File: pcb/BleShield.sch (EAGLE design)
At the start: 11 parts, among them U1 ARDUINO_SHIELDNOHOLES, Y1 32.768KHz, 10PPM

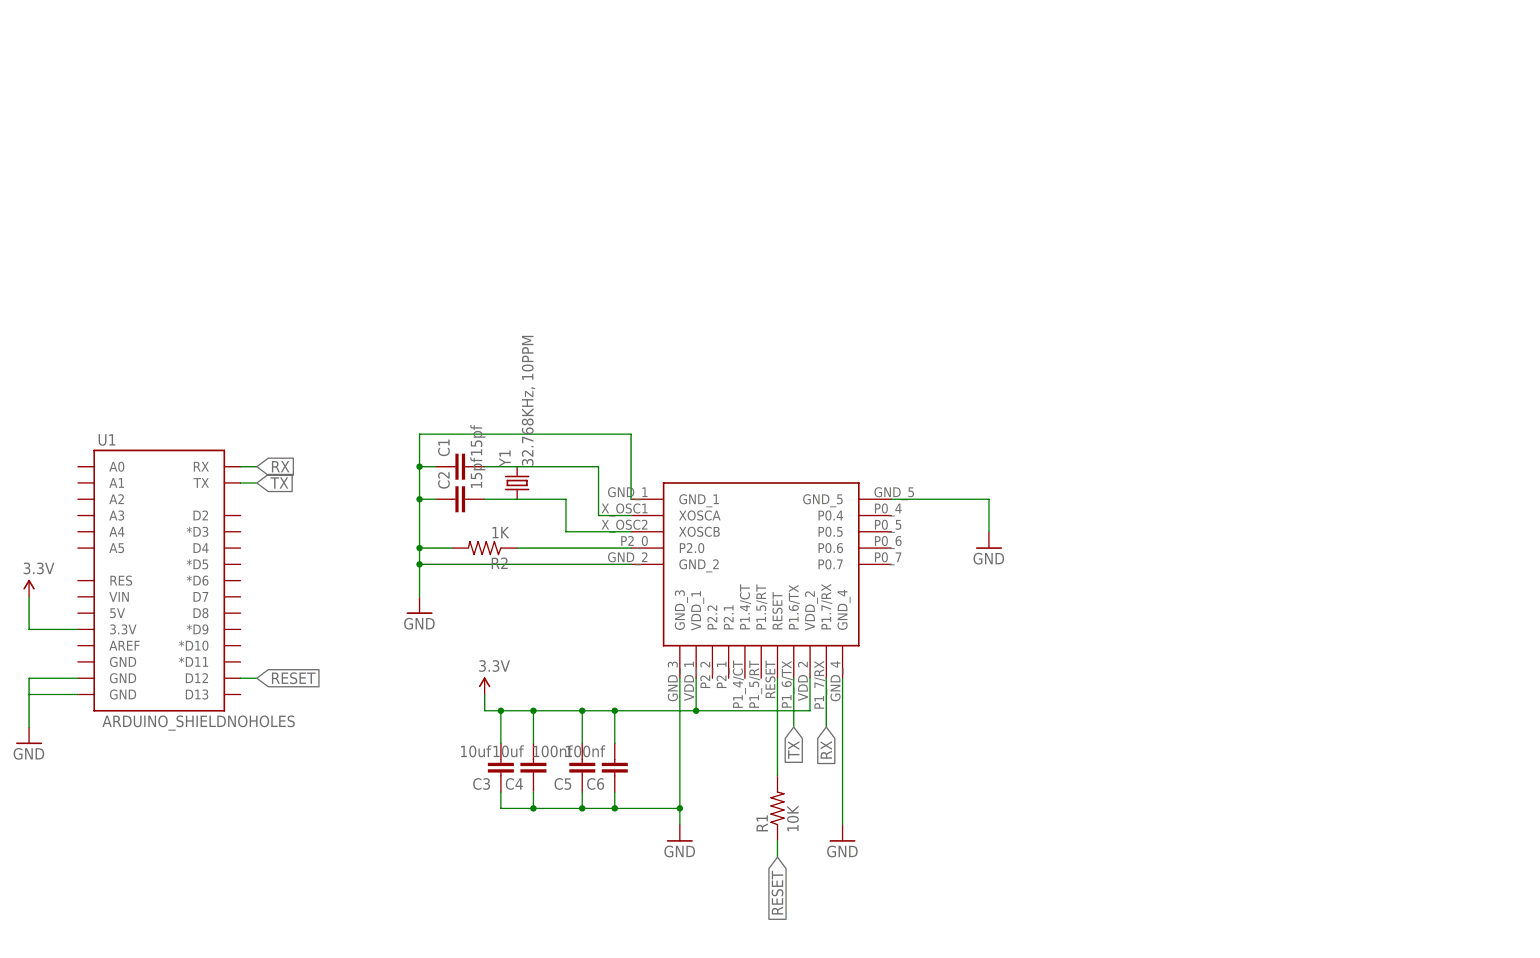
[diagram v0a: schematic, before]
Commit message: Add option to use software serial port, make the board smaller, etc.
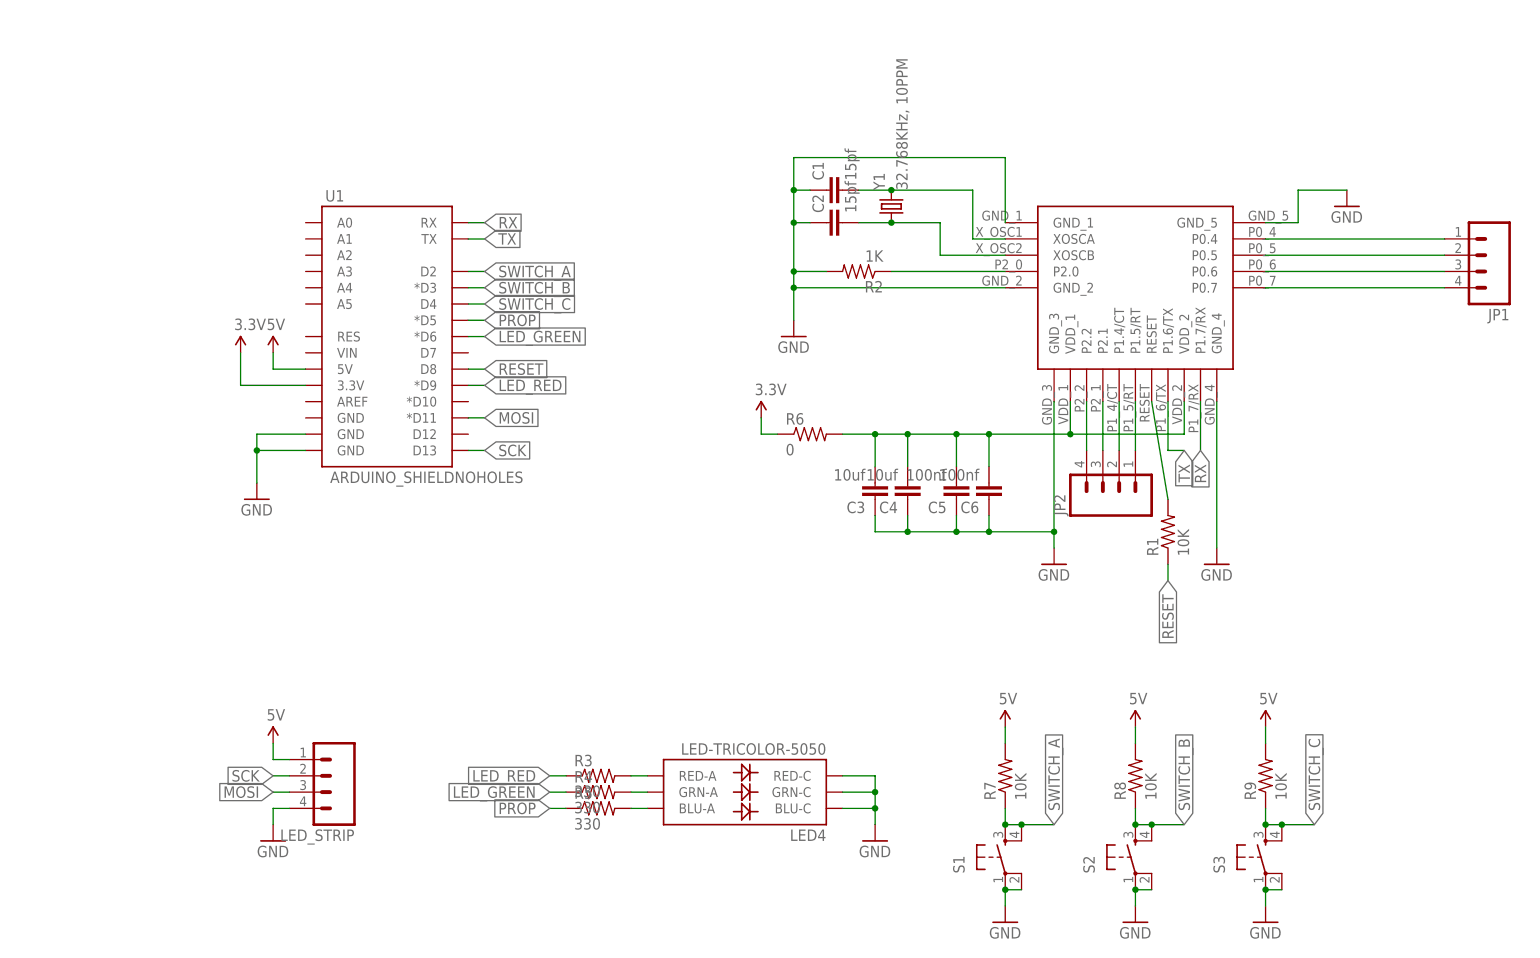
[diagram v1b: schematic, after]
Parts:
- added JP1, JP2, LED_STRIP: (no value), SparkFun:M04PTH
- added LED4: LED-TRICOLOR-5050, SparkFun:LED-TRICOLOR-5050
- added R3, R4, R5: 330, SparkFun:RESISTOR0805-RES
- added R6: 0, SparkFun:RESISTOR0805-RES
- added R7, R8, R9: 10K, SparkFun:RESISTOR0805-RES
- added S1, S2, S3: (no value), SparkFun:TAC_SWITCHSMD
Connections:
- new net 5V: LED_STRIP.1, R7.2, R8.2, R9.2, U1.5V
- new net LED_GREEN: R4.1, U1.*D6
- new net LED_RED: R3.1, U1.*D9
- new net MOSI: LED_STRIP.3, U1.*D11
- new net N$10: JP1.2, U$1.P0.5
- new net N$11: JP1.3, U$1.P0.6
- new net N$12: JP1.4, U$1.P0.7
- new net N$13: JP2.1, U$1.P1.5/RT
- new net N$14: JP2.2, U$1.P1.4/CT
- new net N$15: JP2.3, U$1.P2.1
- new net N$16: JP2.4, U$1.P2.2
- new net N$5: LED4.RED-A, R3.2
- new net N$6: LED4.GRN-A, R4.2
- new net N$7: LED4.BLU-A, R5.2
- new net N$8: C3.2, C4.2, C5.2, C6.2, R6.2, U$1.VDD_1, U$1.VDD_2
- new net N$9: JP1.1, U$1.P0.4
- new net PROP: R5.1, U1.*D5
- new net SCK: LED_STRIP.2, U1.D13
- new net SWITCH_A: R7.1, S1.3, S1.4, U1.D2
- new net SWITCH_B: R8.1, S2.3, S2.4, U1.*D3
- new net SWITCH_C: R9.1, S3.3, S3.4, U1.D4
- net 3.3V: now also R6.1; no longer C3.2, C4.2, C5.2, C6.2, U$1.VDD_1, U$1.VDD_2
- net GND: now also LED4.BLU-C, LED4.GRN-C, LED4.RED-C, LED_STRIP.4, S1.1, S1.2, S2.1, S2.2, S3.1, S3.2
- net RESET: now also U1.D8; no longer U1.D12
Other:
- moved on the sheet: C1, C2, C3, C4, C5, C6, R1, R2, U1, Y1

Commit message: label most of the things
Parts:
- added R10, R11: 0 DNP, SparkFun:RESISTOR0805-RES
- added R12, R13: 0, SparkFun:RESISTOR0805-RES
- JP0: value (none) -> LED_STRIP
- S1: value (none) -> A
- renumbered LED_STRIP to JP0, S2 to B, S3 to C
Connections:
- net PROP renamed LED_BLUE
- new net N$18: R10.2, U1.D2
- new net N$19: R12.2, U1.RX
- new net N$20: R13.2, U1.TX
- new net N$21: R11.2, U1.*D3
- net RX: now also R10.1, R12.1; no longer U1.RX
- net SWITCH_A: now also U1.D4; no longer U1.D2
- net SWITCH_B: now also U1.D12; no longer U1.*D3
- net SWITCH_C: now also U1.D7; no longer U1.D4
- net TX: now also R11.1, R13.1; no longer U1.TX

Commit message: Remove R2 resistor
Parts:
- removed R2: 1K, SparkFun:RESISTOR0805-RES
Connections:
- removed net N$2: R2.1, U$1.P2.0
- net GND: no longer R2.2
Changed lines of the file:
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@@
 <?xml version="1.0" encoding="utf-8"?>
 <!DOCTYPE eagle SYSTEM "eagle.dtd">
-<eagle version="6.2">
+<eagle version="6.4">
 <drawing>
 <settings>
@@
 <part name="GND3" library="SparkFun" deviceset="GND" device=""/>
 <part name="R1" library="SparkFun" deviceset="RESISTOR" device="0805-RES" value="10K"/>
-<part name="R2" library="SparkFun" deviceset="RESISTOR" device="0805-RES" value="1K"/>
 <part name="GND4" library="SparkFun" deviceset="GND" device=""/>
 <part name="GND5" library="SparkFun" deviceset="GND" device=""/>
@@
 <instance part="GND3" gate="1" x="101.6" y="99.06"/>
 <instance part="R1" gate="G$1" x="160.02" y="68.58" rot="R90"/>
-<instance part="R2" gate="G$1" x="111.76" y="109.22" rot="R180"/>
 <instance part="GND4" gate="1" x="187.96" y="119.38"/>
 <instance part="GND5" gate="1" x="167.64" y="63.5"/>
@@
 <wire x1="101.6" y1="127" x2="101.6" y2="121.92" width="0.1524" layer="91"/>
 <junction x="101.6" y="106.68"/>
-<pinref part="R2" gate="G$1" pin="2"/>
 <wire x1="101.6" y1="121.92" x2="101.6" y2="116.84" width="0.1524" layer="91"/>
-<wire x1="101.6" y1="116.84" x2="101.6" y2="109.22" width="0.1524" layer="91"/>
-<wire x1="101.6" y1="109.22" x2="101.6" y2="106.68" width="0.1524" layer="91"/>
-<wire x1="106.68" y1="109.22" x2="101.6" y2="109.22" width="0.1524" layer="91"/>
-<junction x="101.6" y="109.22"/>
+<wire x1="101.6" y1="116.84" x2="101.6" y2="106.68" width="0.1524" layer="91"/>
 <pinref part="C1" gate="G$1" pin="1"/>
 <wire x1="104.14" y1="121.92" x2="101.6" y2="121.92" width="0.1524" layer="91"/>
@@
 </segment>
 </net>
-<net name="N$2" class="0">
-<segment>
-<pinref part="U$1" gate="G$1" pin="P2.0"/>
-<pinref part="R2" gate="G$1" pin="1"/>
-<wire x1="134.62" y1="109.22" x2="116.84" y2="109.22" width="0.1524" layer="91"/>
-</segment>
-</net>

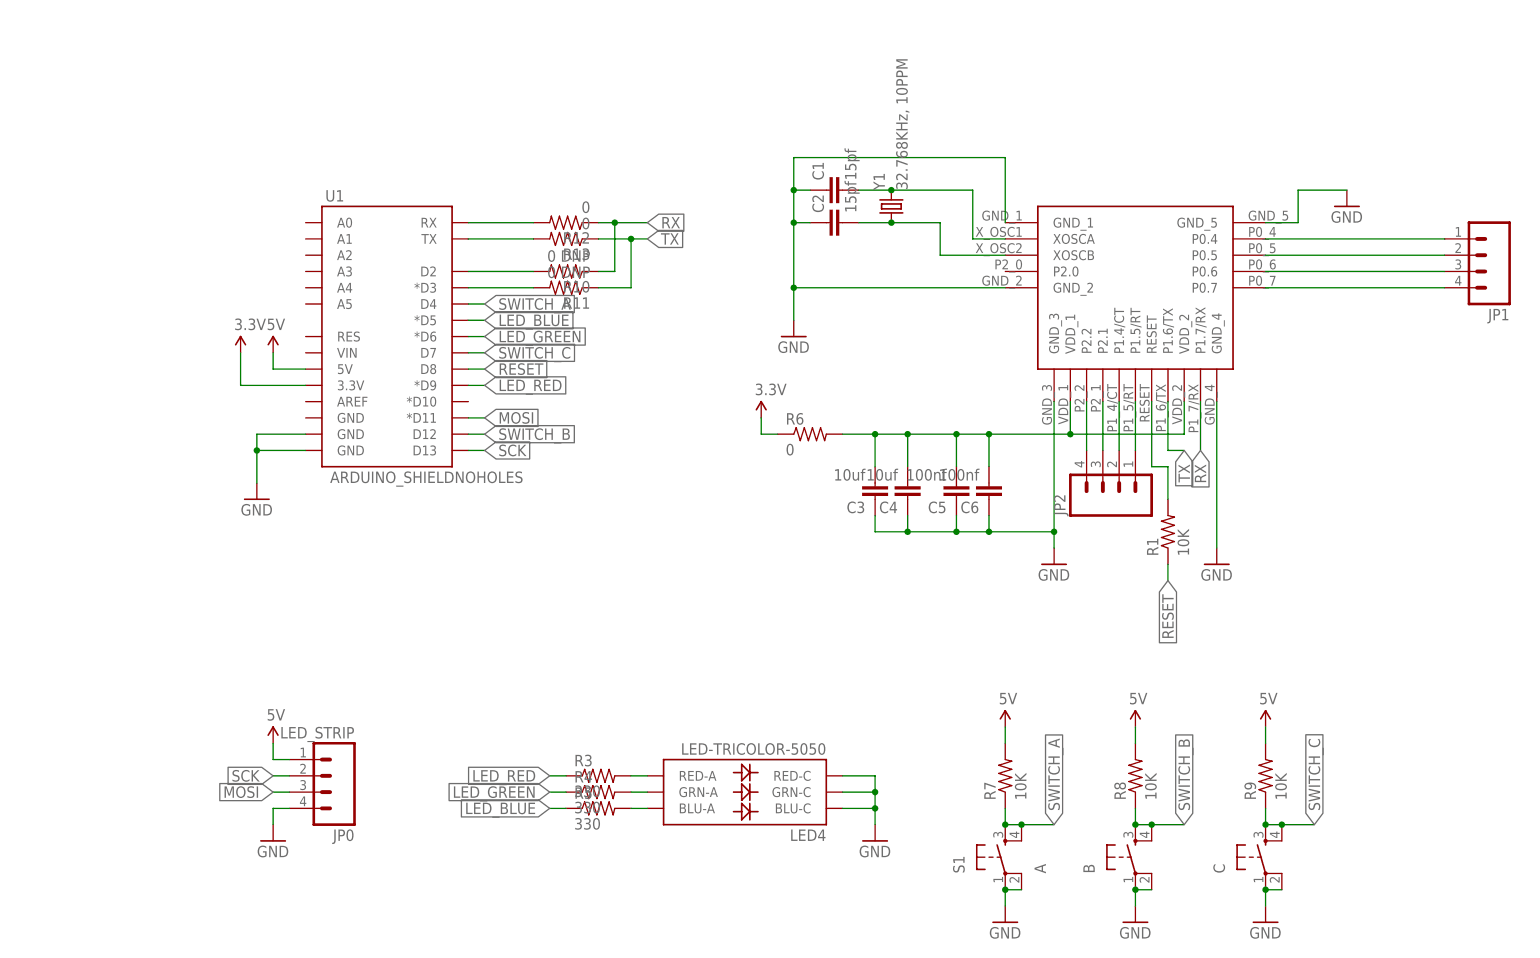
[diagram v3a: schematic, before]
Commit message: fixed LED pinout, changed crystal to 3225 package
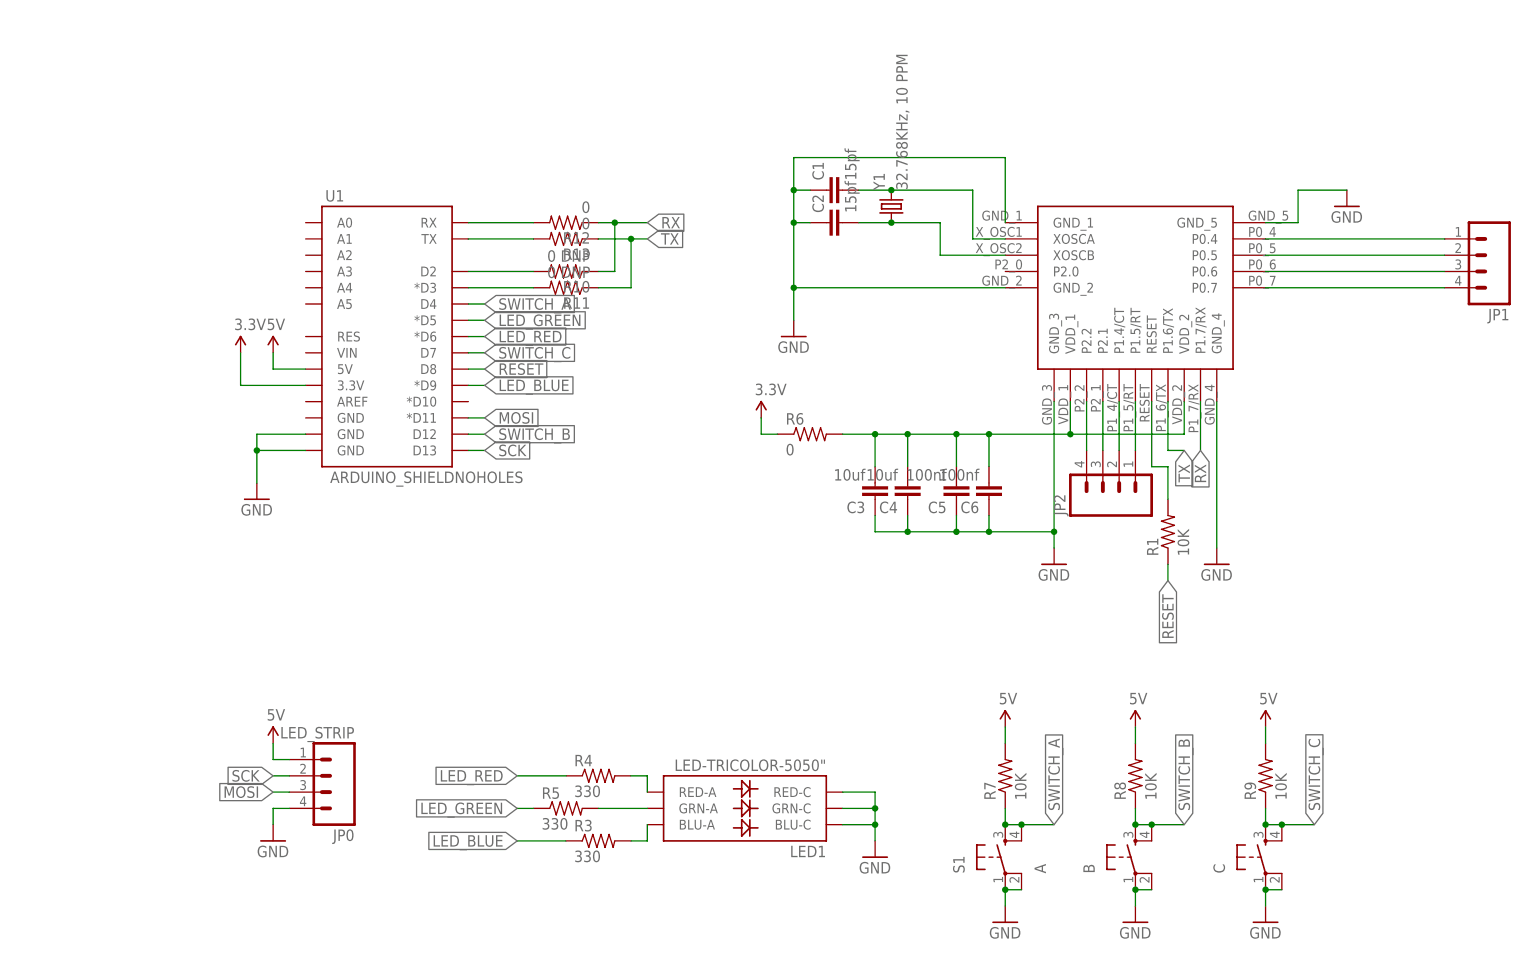
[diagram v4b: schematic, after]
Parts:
- removed LED4: LED-TRICOLOR-5050, SparkFun:LED-TRICOLOR-5050
- added LED1: LED-TRICOLOR-5050", blinkiverse:LED-TRICOLOR-5050"
- Y1: value 32.768KHz, 10PPM -> 32.768KHz, 10 PPM; device SparkFun:CRYSTAL32-SMD -> blinkiverse:CRYSTAL
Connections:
- removed net N$7: LED4.BLU-A, R5.2
- new net N$2: LED1.BLU-A, R3.2
- net GND: now also LED1.BLU-C, LED1.GRN-C, LED1.RED-C; no longer LED4.BLU-C, LED4.GRN-C, LED4.RED-C
- net LED_BLUE: now also R3.1, U1.*D9; no longer R5.1, U1.*D5
- net LED_GREEN: now also R5.1, U1.*D5; no longer R4.1, U1.*D6
- net LED_RED: now also R4.1, U1.*D6; no longer R3.1, U1.*D9
- net N$5: now also LED1.GRN-A, R5.2; no longer LED4.RED-A, R3.2
- net N$6: now also LED1.RED-A; no longer LED4.GRN-A
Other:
- moved on the sheet: R3, R4, R5

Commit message: fixed silkscreens, minor re-routing, added teardrops
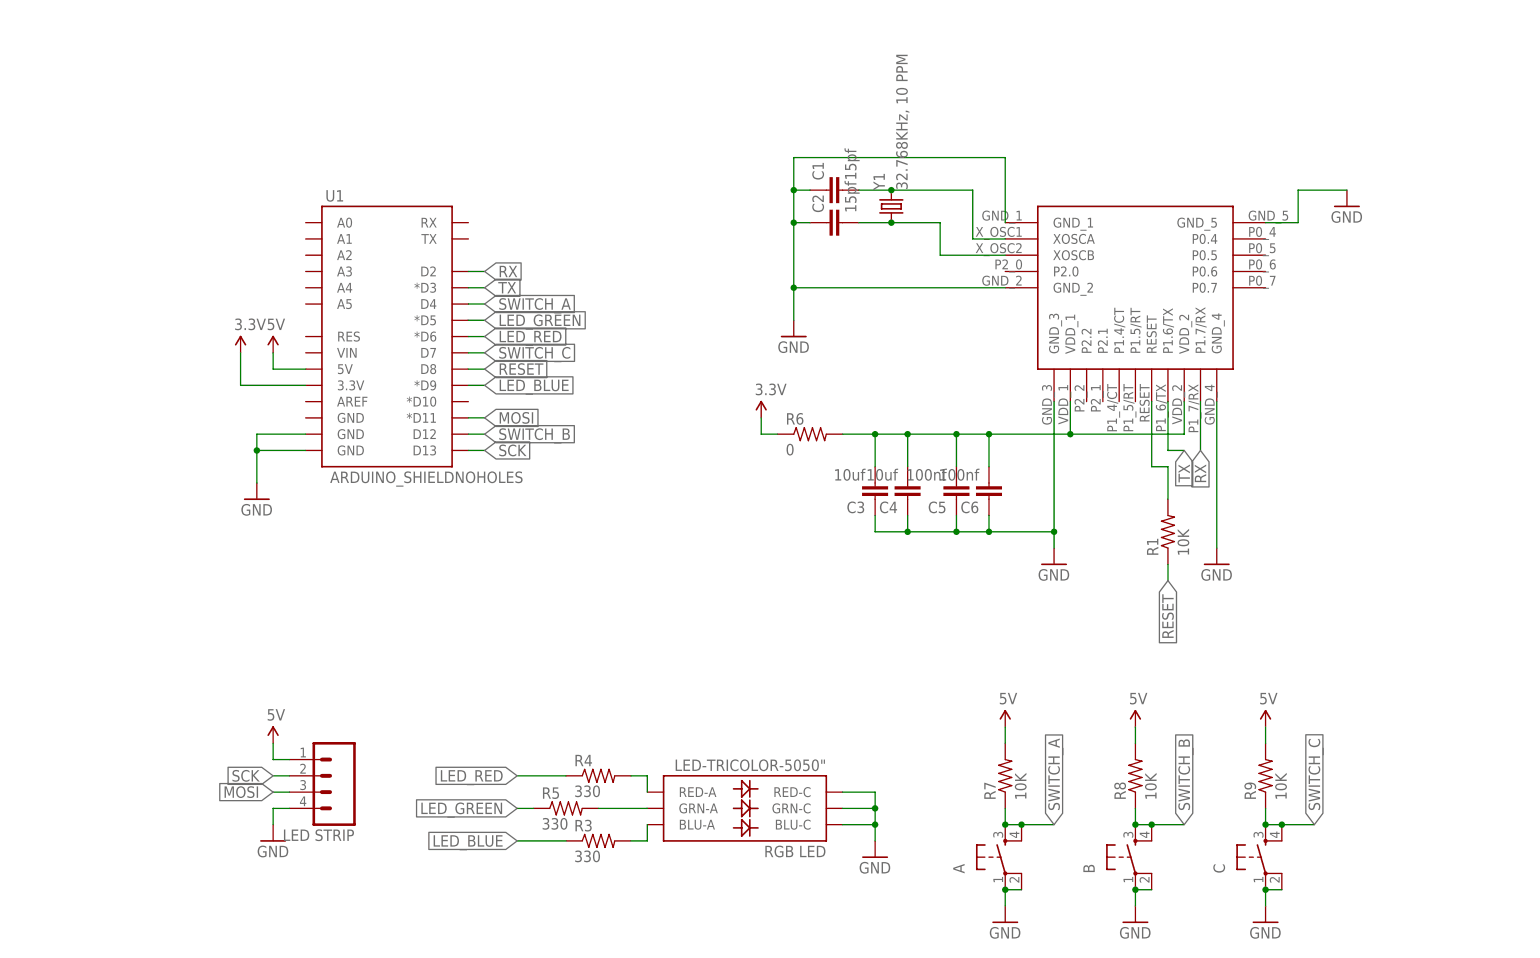
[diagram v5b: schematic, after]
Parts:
- LED STRIP: renamed from JP0
- RGB LED: renamed from LED1
- removed JP1, JP2: (no value), SparkFun:M04PTH
- removed R10, R11: 0 DNP, SparkFun:RESISTOR0805-RES
- removed R12, R13: 0, SparkFun:RESISTOR0805-RES
- A: value A -> (none)
- LED STRIP: value LED_STRIP -> (none)
- renumbered S1 to A
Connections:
- removed net N$10: JP1.2, U$1.P0.5
- removed net N$11: JP1.3, U$1.P0.6
- removed net N$12: JP1.4, U$1.P0.7
- removed net N$13: JP2.1, U$1.P1.5/RT
- removed net N$14: JP2.2, U$1.P1.4/CT
- removed net N$15: JP2.3, U$1.P2.1
- removed net N$16: JP2.4, U$1.P2.2
- removed net N$18: R10.2, U1.D2
- removed net N$19: R12.2, U1.RX
- removed net N$20: R13.2, U1.TX
- removed net N$21: R11.2, U1.*D3
- removed net N$9: JP1.1, U$1.P0.4
- net RX: now also U1.D2; no longer R10.1, R12.1
- net TX: now also U1.*D3; no longer R11.1, R13.1
